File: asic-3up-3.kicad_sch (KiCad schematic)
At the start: 80 parts, among them J10 Conn_01x01, J11 Conn_01x01, J21 Conn_01x01, U4 SN74AVC4T774, U5 25MHz, U66 MCP1824T-1202E/OT, U67 MCP1824T-1202E/OT, U68 MCP1824T-1202E/OT, U69 MCP1824T-0802E, U70 MCP1824T-0802E, U71 MCP1824T-0802E, U72 BM1362AC_MODE1, U73 BM1362AC_MODE0, U74 BM1362AC_MODE1

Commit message: DNP low side FET snubber circuit for now (to be redone in v4). Update current sense resistor filter values. regenerate BOM, iBOM. Slight slikscreen cleanup. regenerated gerbers
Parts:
- J10, J11, J21: now left out of the parts list
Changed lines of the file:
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@@
 		(unit 1)
 		(exclude_from_sim no)
-		(in_bom yes)
+		(in_bom no)
 		(on_board yes)
 		(dnp no)
@@
 		(unit 1)
 		(exclude_from_sim no)
-		(in_bom yes)
+		(in_bom no)
 		(on_board yes)
 		(dnp no)
@@
 		(unit 1)
 		(exclude_from_sim no)
-		(in_bom yes)
-		(on_board yes)
-		(dnp no)
+		(in_bom no)
+		(on_board yes)
+		(dnp no)

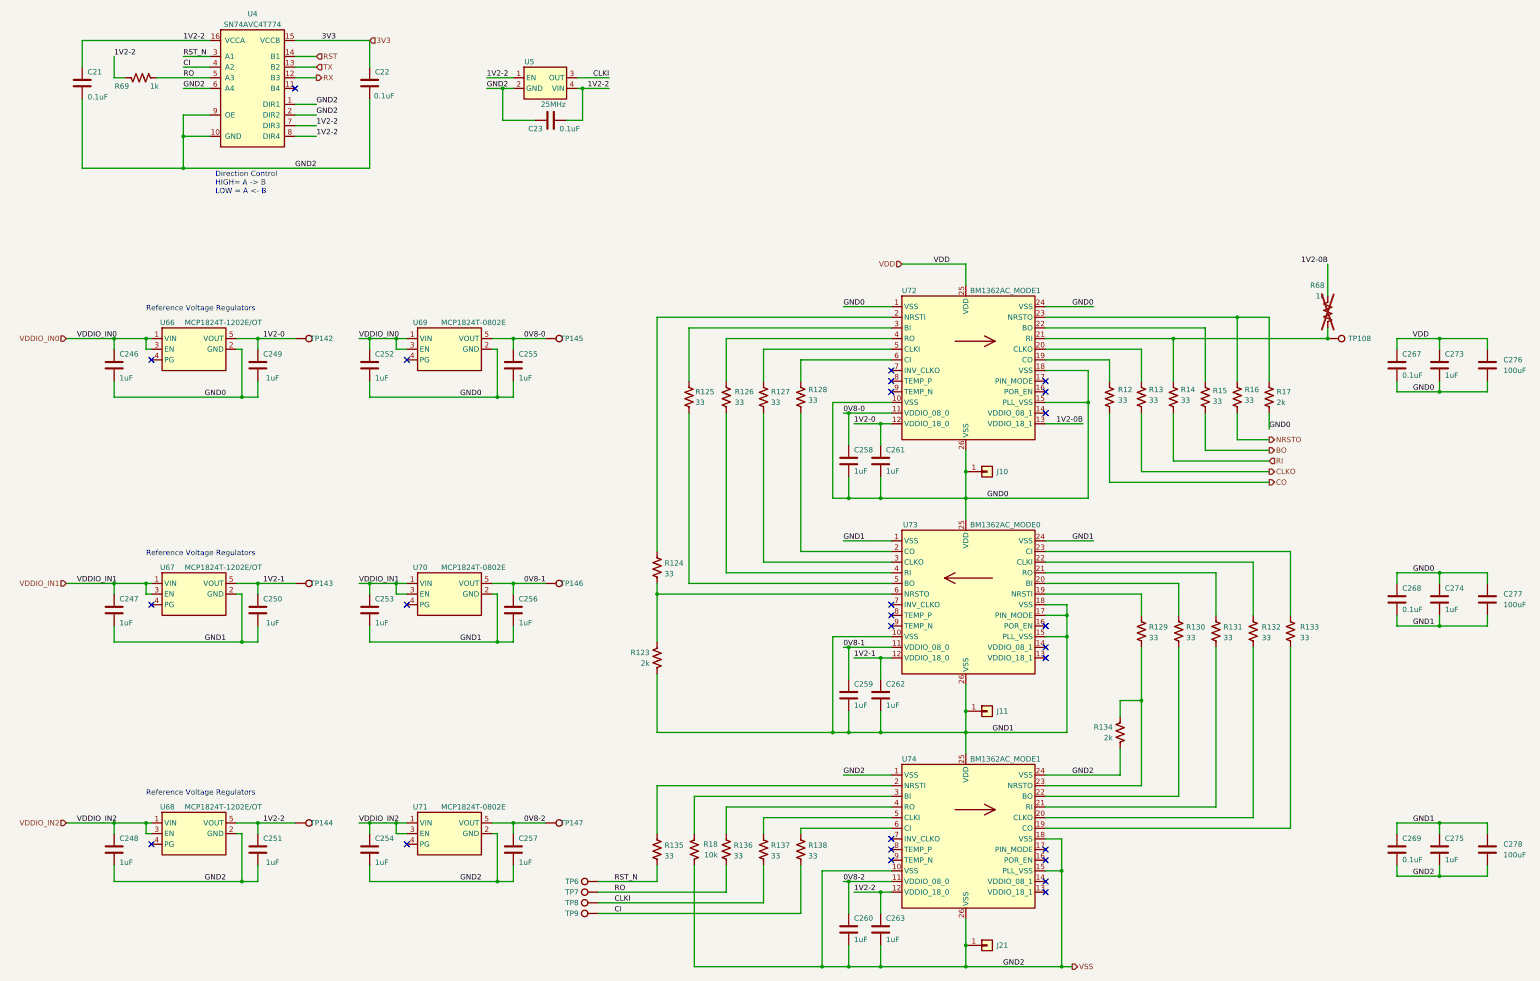
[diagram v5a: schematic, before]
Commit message: Added Mfg to BOM
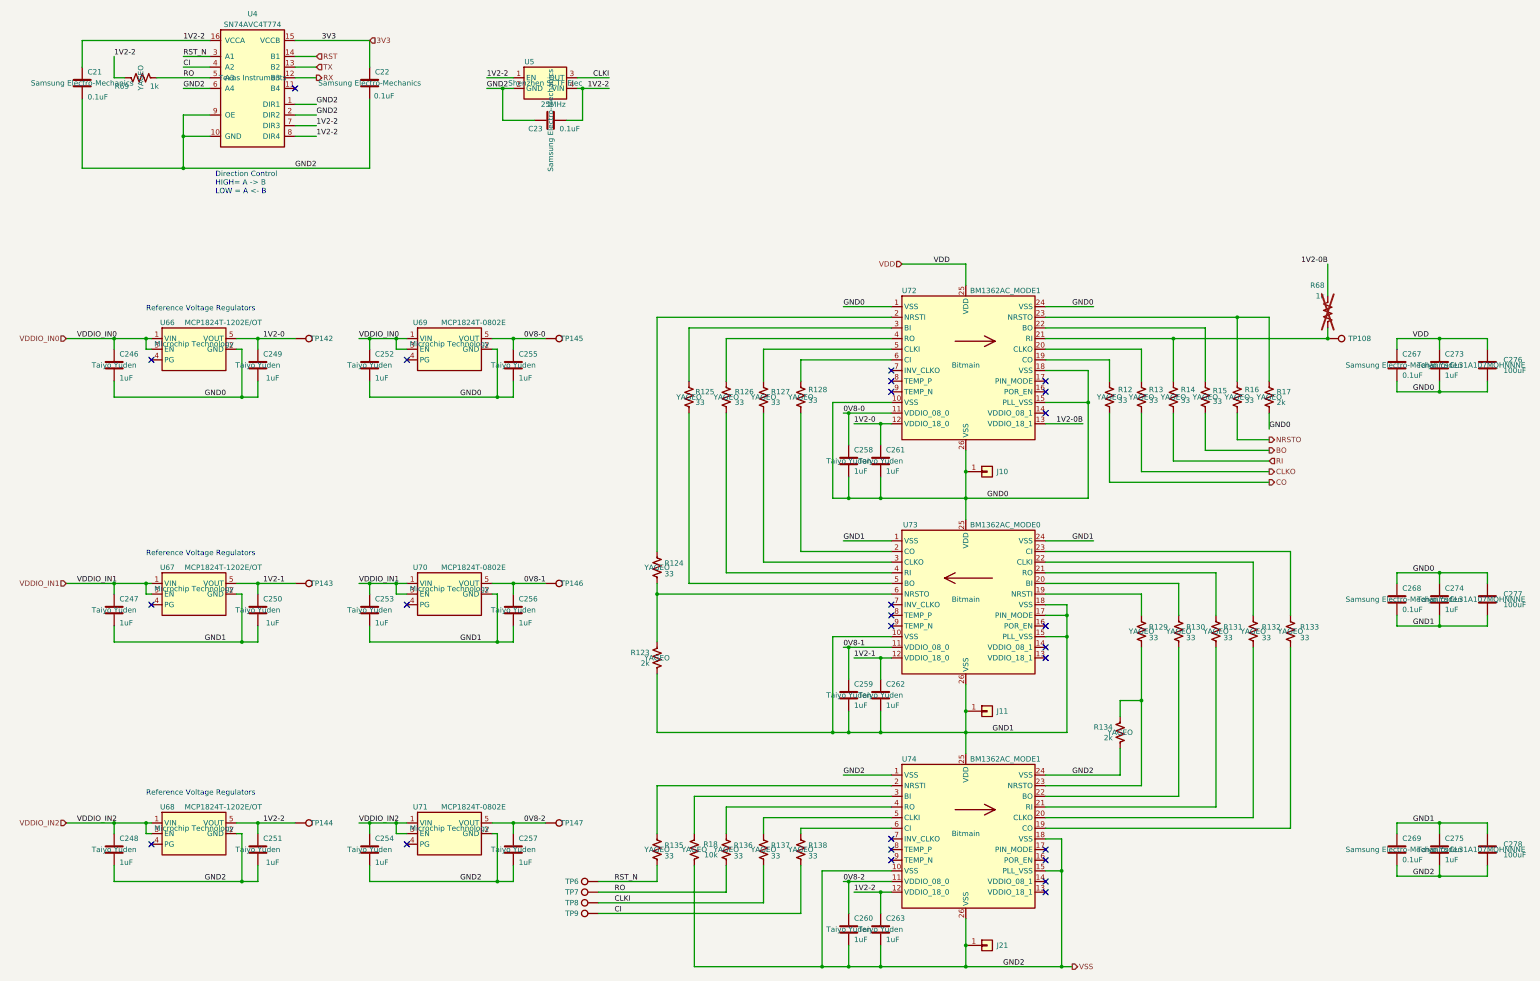
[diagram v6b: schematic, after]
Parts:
- C21, C22, C23, C267, C268, C269: Manufacturer (none) -> Samsung Electro-Mechanics
- C246, C247, C248, C249, C250, C251, C252, C253, C254, C255, C256, C257, C258, C259, C260, C261, C262, C263, C273, C274, C275: Manufacturer (none) -> Taiyo Yuden
- C276, C277, C278: Manufacturer (none) -> CL31A107MQHNNNE
- R12, R123, R124, R125, R126, R127, R128, R129, R13, R130, R131, R132, R133, R134, R135, R136, R137, R138, R14, R15, R16, R17, R18, R69: Manufacturer (none) -> YAGEO
- U4: Manufacturer (none) -> Texas Instruments
- U5: Manufacturer (none) -> Shenzhen SCTF Elec
- U66, U67, U68, U69, U70, U71: Manufacturer (none) -> Microchip Technology
- U72, U73, U74: Manufacturer (none) -> Bitmain

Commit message: missed a few
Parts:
- U72, U73, U74: PARTNO (none) -> BM1362AC
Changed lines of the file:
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@@
+			)
+		)
+		(property "PARTNO" "BM1362AC"
+			(at 260.35 111.76 0)
+			(effects
+				(font
+					(size 1.27 1.27)
+				)
 			)
 		)
@@
 			)
 		)
+		(property "PARTNO" "BM1362AC"
+			(at 260.35 167.64 0)
+			(effects
+				(font
+					(size 1.27 1.27)
+				)
+			)
+		)
 		(pin "10"
 		)
@@
 			(at 260.35 223.52 0)
 			(effects
+				(font
+					(size 1.27 1.27)
+				)
+			)
+		)
+		(property "PARTNO" "BM1362AC"
+			(at 260.35 223.52 0)
+			(effects

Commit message: fixed wrong part number
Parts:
- R69: PARTNO RC0402FR-072KL -> RC0402FR-071KL
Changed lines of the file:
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@@
 			)
 		)
-		(property "PARTNO" "RC0402FR-072KL"
+		(property "PARTNO" "RC0402FR-071KL"
 			(at 63.5 43.18 0)
 			(effects
